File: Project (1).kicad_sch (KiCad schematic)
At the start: 8 parts, among them U1 DRV8833PW, U2 DRV8833PW, U3 INA219AxD, U4 SiP32431DR3, U5 TP4056, U6 TPS61090RSAR, U7 TPS62933DRLR, U8 CH224K

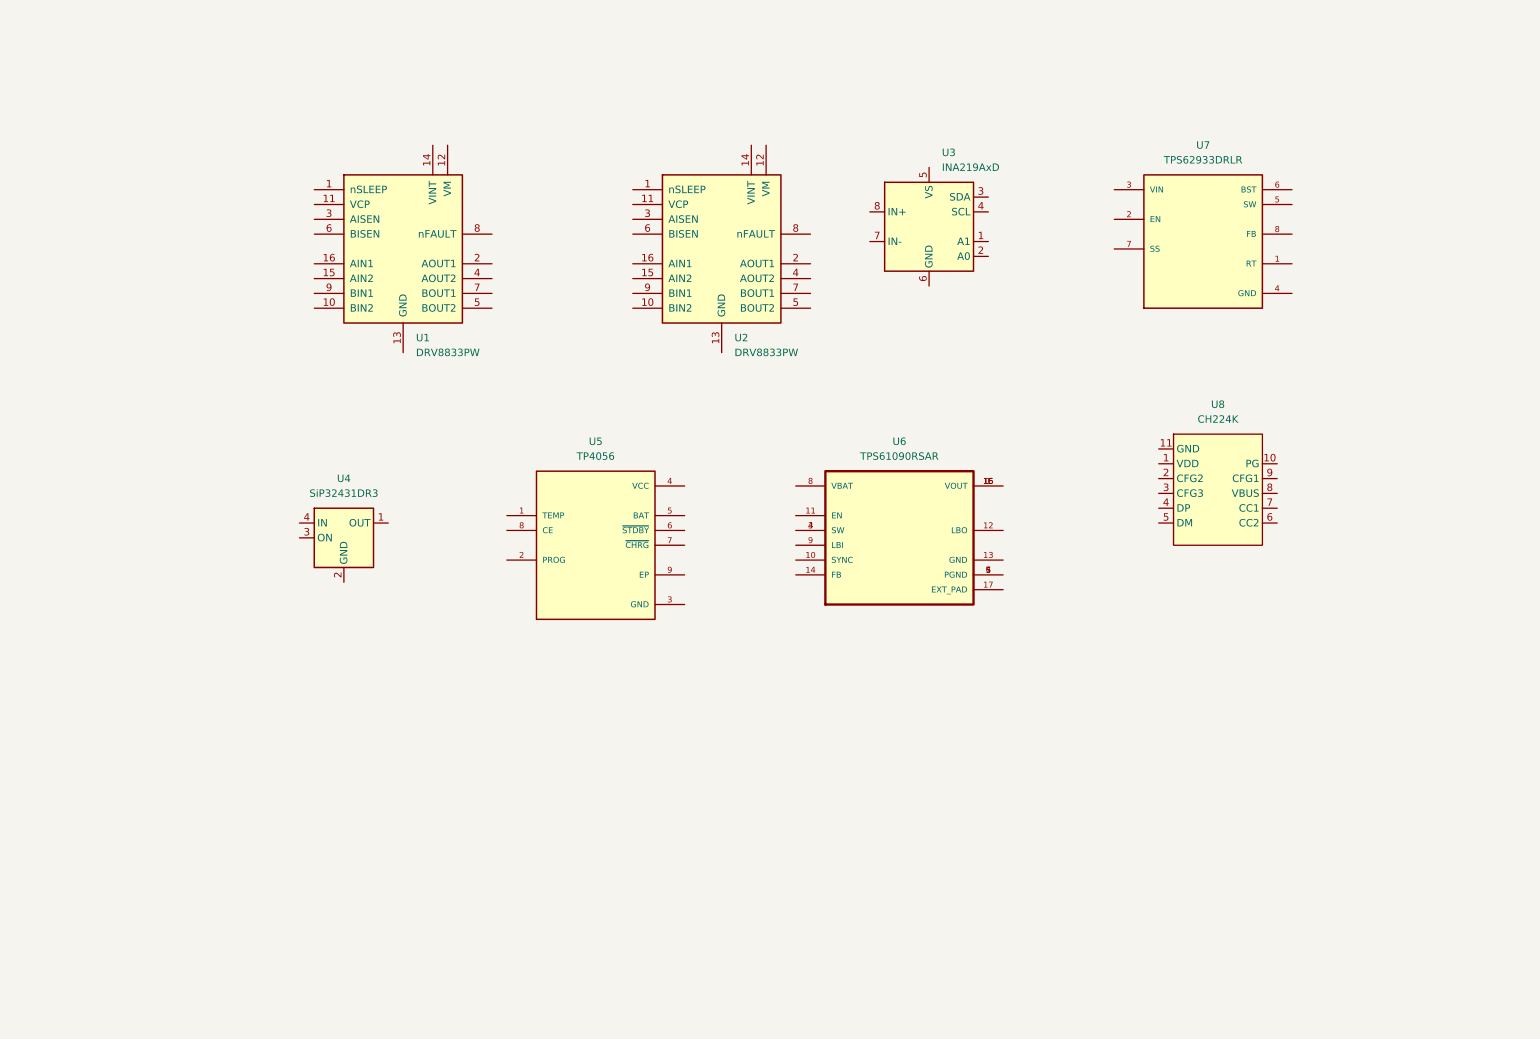
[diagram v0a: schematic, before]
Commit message: Added connector and labels for connector
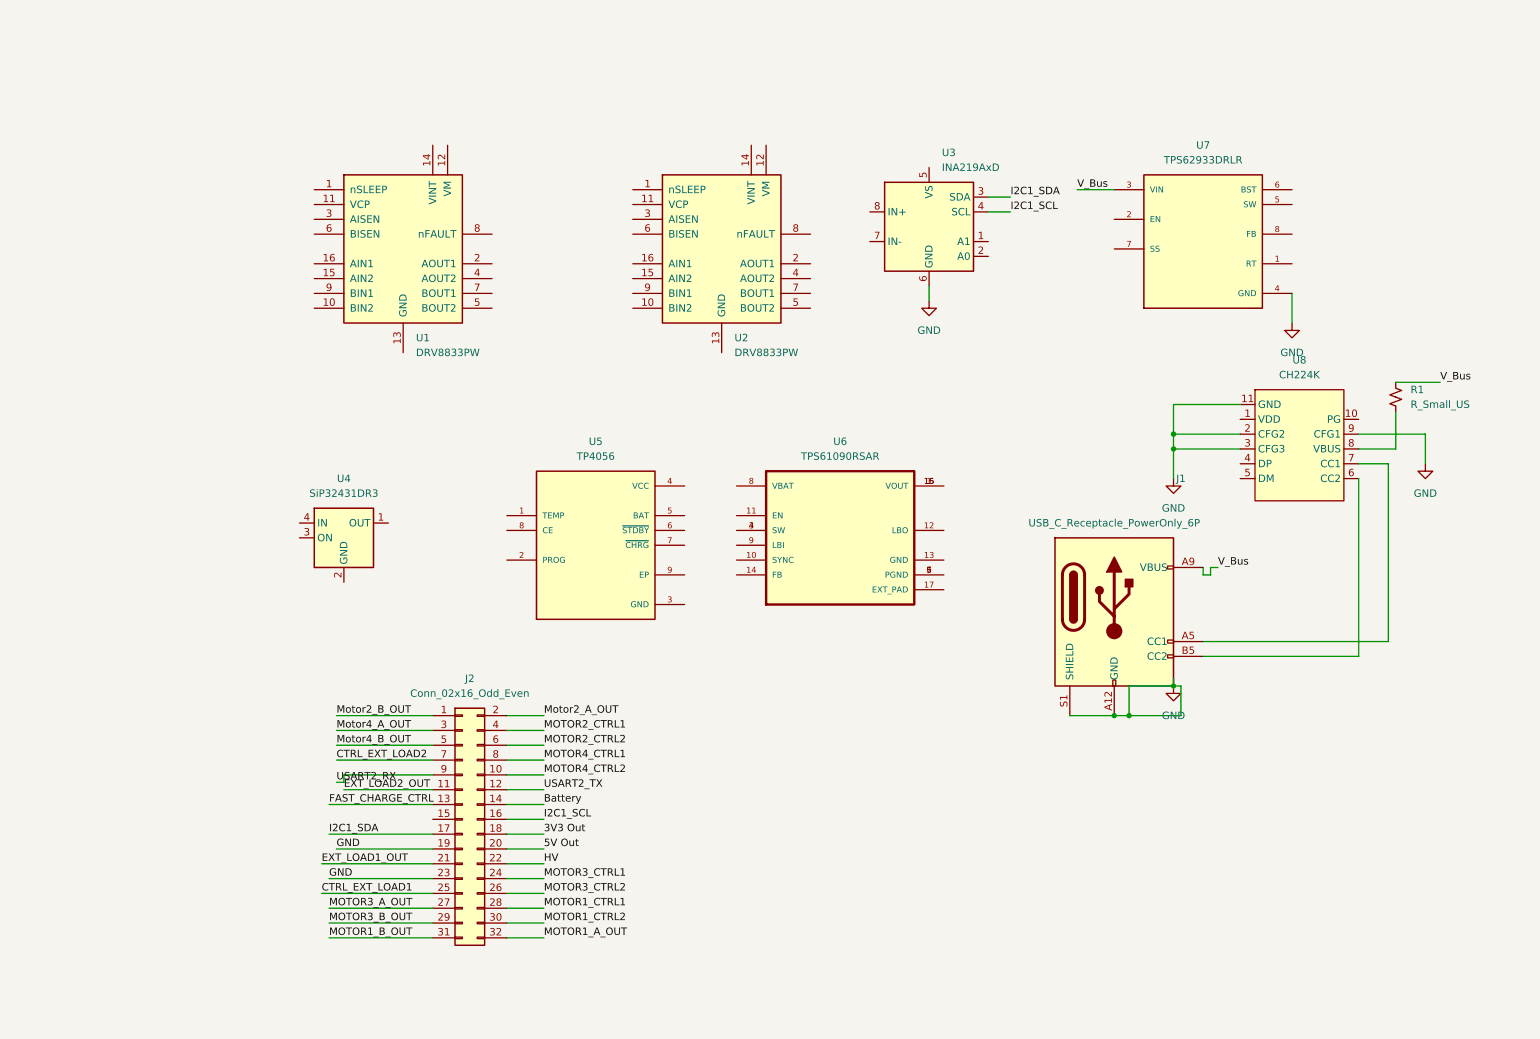
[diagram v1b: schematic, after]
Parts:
- added J1: USB_C_Receptacle_PowerOnly_6P, symbol Connector:USB_C_Receptacle_PowerOnly_6P
- added J2: Conn_02x16_Odd_Even, symbol Connector_Generic:Conn_02x16_Odd_Even
- added R1: R_Small_US, symbol Device:R_Small_US
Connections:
- net GND: now reaches U8.11 (GND)
- net GND: now also U3.6 (GND), U7.4 (GND), U8.2 (CFG2), U8.3 (CFG3), U8.9 (CFG1), J1.A12 (GND), J1.B12 (GND), J1.S1 (SHIELD), J2.23 (Pin_23)
- net at U8.6 (CC2): now also J1.B5 (CC2)
- net at U8.7 (CC1): now also J1.A5 (CC1)
- net at U8.8 (VBUS): now also R1.2
- net I2C1_SDA: now reaches U3.3 (SDA)
- net I2C1_SDA: now also J2.17 (Pin_17)
- net I2C1_SCL : now reaches U3.4 (SCL)
- net V_Bus: now reaches U7.3 (VIN)
- net V_Bus: now also J1.A9 (VBUS), J1.B9 (VBUS), R1.1
- new net 3V3 Out : J2.18 (Pin_18)
- new net 5V Out: J2.20 (Pin_20)
- new net Battery: J2.14 (Pin_14)
- new net CTRL_EXT_LOAD1: J2.25 (Pin_25)
- new net CTRL_EXT_LOAD2  : J2.7 (Pin_7)
- new net EXT_LOAD1_OUT: J2.21 (Pin_21)
- new net EXT_LOAD2_OUT: J2.11 (Pin_11)
- new net FAST_CHARGE_CTRL: J2.13 (Pin_13)
- new net GND : J2.19 (Pin_19)
- new net HV: J2.22 (Pin_22)
- new net I2C1_SCL: J2.16 (Pin_16)
- new net MOTOR1_A_OUT: J2.32 (Pin_32)
- new net MOTOR1_B_OUT: J2.31 (Pin_31)
- new net MOTOR1_CTRL1: J2.28 (Pin_28)
- new net MOTOR1_CTRL2: J2.30 (Pin_30)
- new net MOTOR2_CTRL1: J2.4 (Pin_4)
- new net MOTOR2_CTRL2 : J2.6 (Pin_6)
- new net MOTOR3_A_OUT: J2.27 (Pin_27)
- new net MOTOR3_B_OUT: J2.29 (Pin_29)
- new net MOTOR3_CTRL1: J2.24 (Pin_24)
- new net MOTOR3_CTRL2: J2.26 (Pin_26)
- new net MOTOR4_CTRL1: J2.8 (Pin_8)
- new net MOTOR4_CTRL2: J2.10 (Pin_10)
- new net Motor2_A_OUT: J2.2 (Pin_2)
- new net Motor2_B_OUT : J2.1 (Pin_1)
- new net Motor4_A_OUT : J2.3 (Pin_3)
- new net Motor4_B_OUT : J2.5 (Pin_5)
- new net USART2_RX: J2.9 (Pin_9)
- new net USART2_TX: J2.12 (Pin_12)
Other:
- moved on the sheet: U6, U8

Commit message: Added motor driver labels
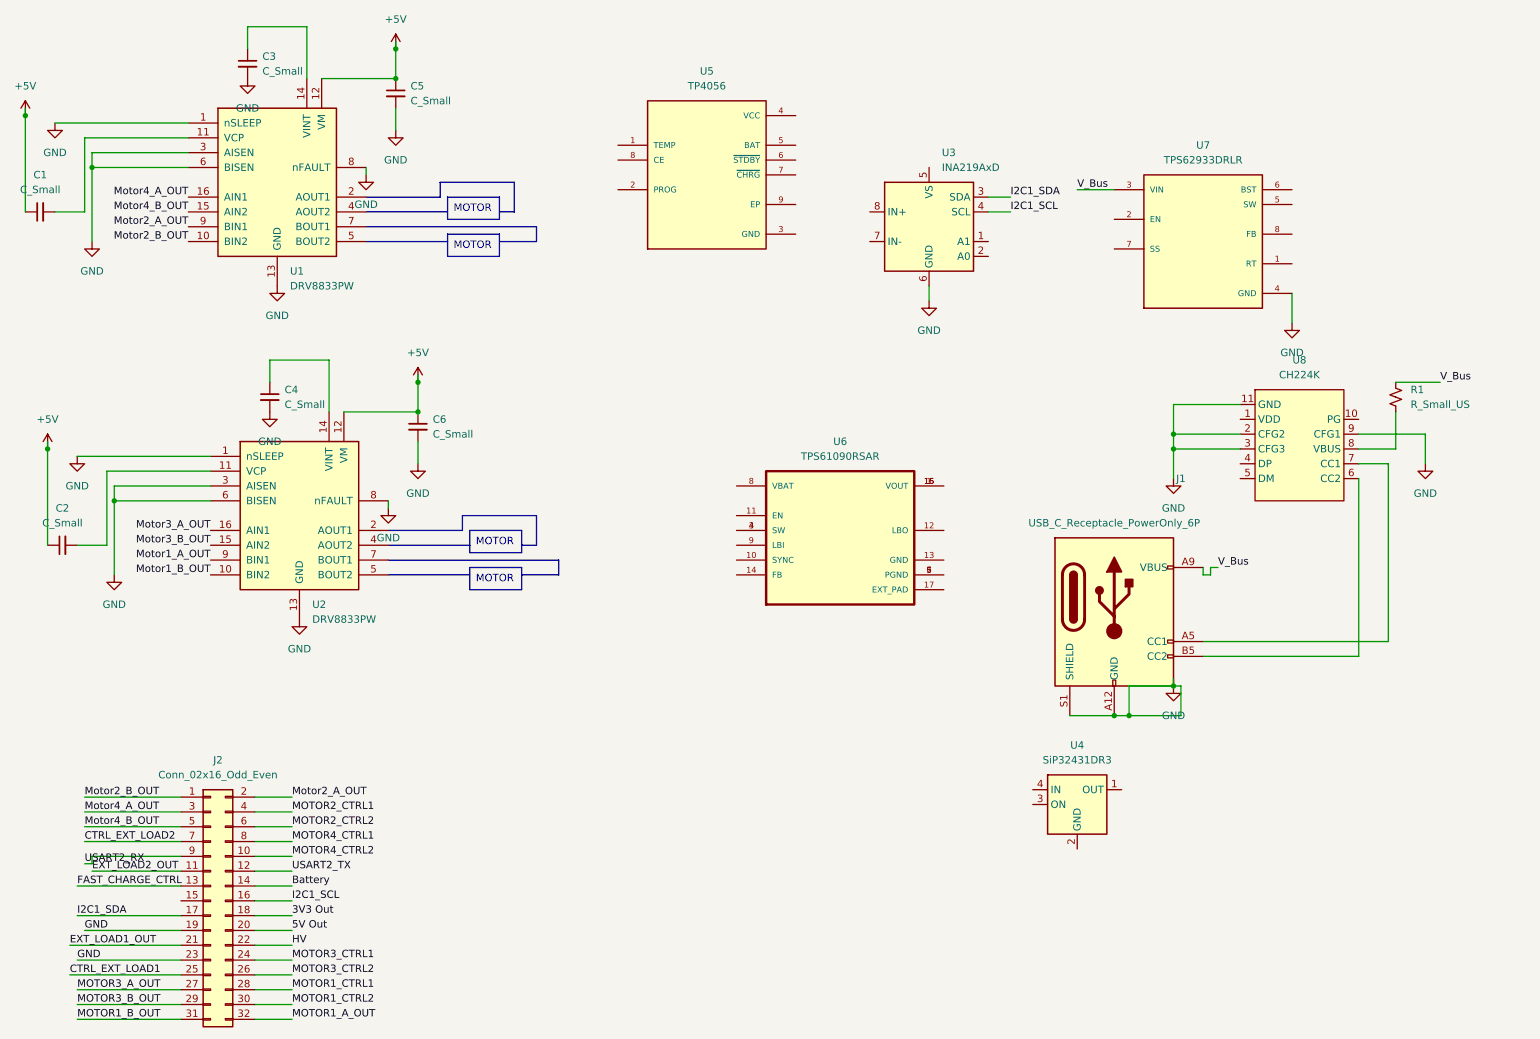
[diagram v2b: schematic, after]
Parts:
- added C1, C2, C3, C4, C5, C6: C_Small, symbol Device:C_Small
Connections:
- net GND: now also U1.1 (nSLEEP), U1.13 (GND), U1.3 (AISEN), U1.6 (BISEN), U1.8 (nFAULT), U2.1 (nSLEEP), U2.13 (GND), U2.3 (AISEN), U2.6 (BISEN), U2.8 (nFAULT), C3.2, C4.2, C5.2, C6.2
- net Motor2_A_OUT: now also U1.9 (BIN1)
- net Motor1_B_OUT: now reaches U2.10 (BIN2)
- net at U2.11 (VCP): now also C2.2
- net +5V: now reaches U2.12 (VM)
- net +5V: now also U1.12 (VM), C1.1, C2.1, C5.1, C6.1
- net at U2.14 (VINT): now also C4.1
- net Motor3_B_OUT: now reaches U2.15 (AIN2)
- net Motor3_A_OUT: now reaches U2.16 (AIN1)
- net Motor1_A_OUT: now reaches U2.9 (BIN1)
- net Motor2_B_OUT: now reaches U1.10 (BIN2)
- net at U1.11 (VCP): now also C1.2
- net at U1.14 (VINT): now also C3.1
- net Motor4_B_OUT: now reaches U1.15 (AIN2)
- net Motor4_A_OUT: now reaches U1.16 (AIN1)
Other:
- moved on the sheet: J2, U4, U5

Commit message: updated INA219
added labels and connections
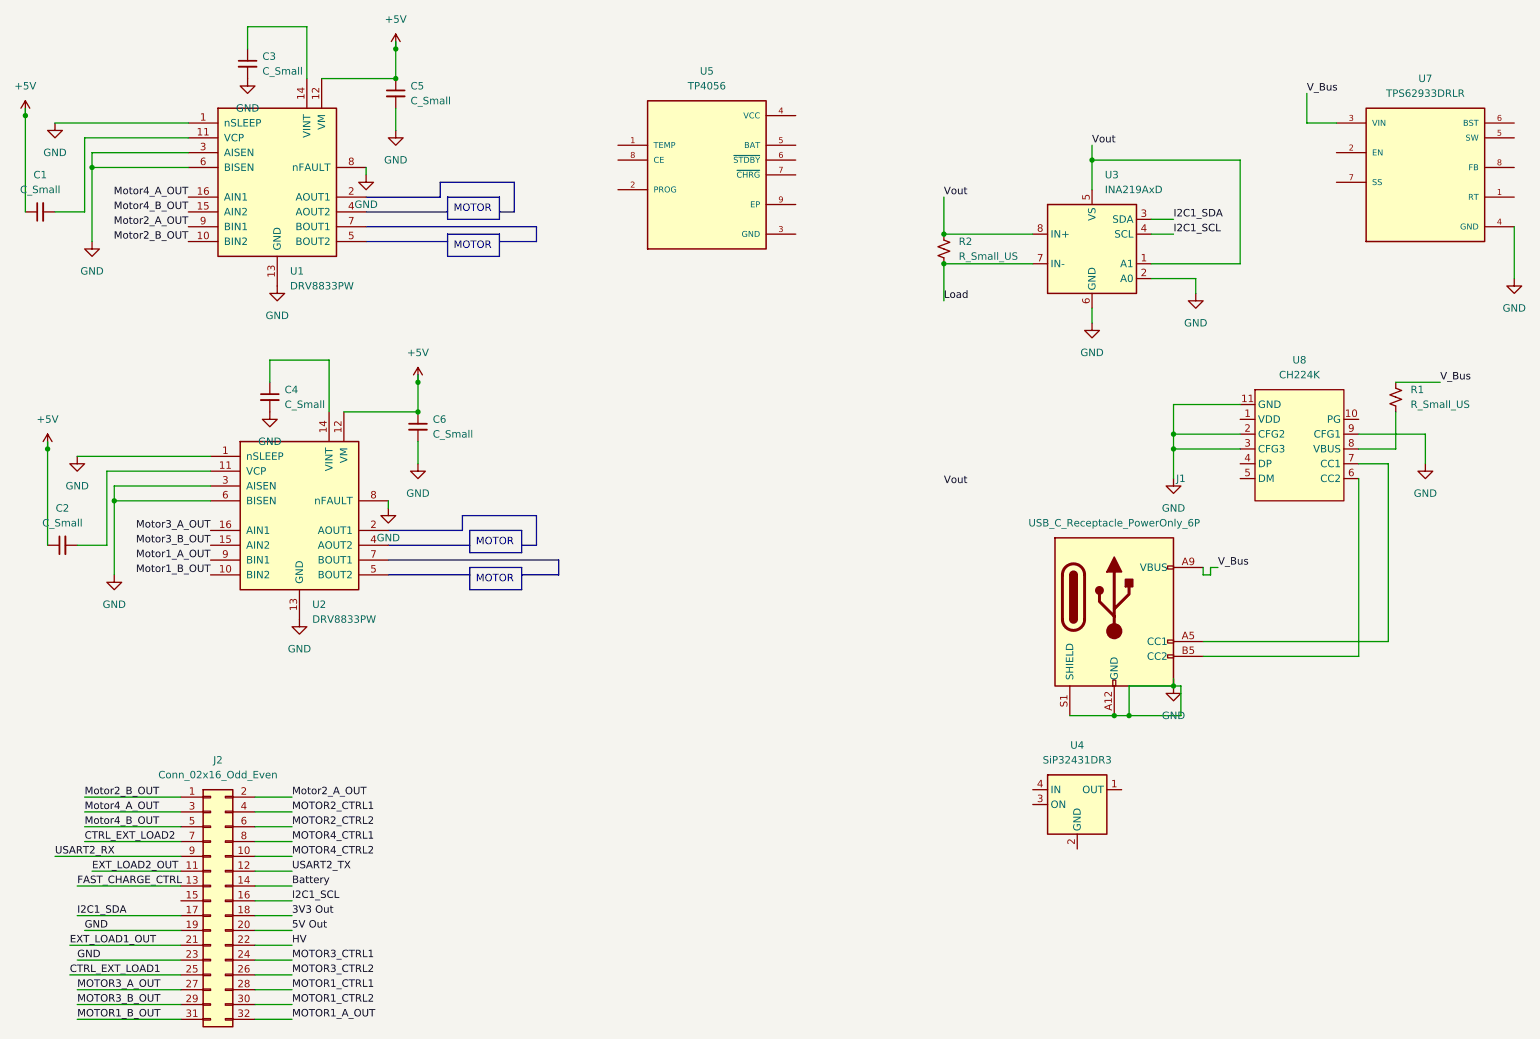
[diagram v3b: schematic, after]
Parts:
- removed U6: TPS61090RSAR, TPS61090RSAR:QFN65P400X400X100-17N, symbol TPS61090RSAR:TPS61090RSAR
- added R2: R_Small_US, symbol Device:R_Small_US
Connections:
- net GND: now also U3.2 (A0)
- net Vout: now reaches U3.1 (A1)
- net Vout: now also U3.5 (VS), U3.8 (IN+), R2.1
- net Load: now reaches U3.7 (IN-)
- net Load: now also R2.2
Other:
- moved on the sheet: U3, U7
